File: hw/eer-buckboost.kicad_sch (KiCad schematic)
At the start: 58 parts, among them IC2001 LTC3779IFE#PBF, Q2001 BSC360N15NS3 G, Q2002 BSC360N15NS3 G, Q2003 BSC360N15NS3 G, Q2004 BSC360N15NS3 G, U2001 NVTFS6H888NLTAG, U2002 TLV9062xD

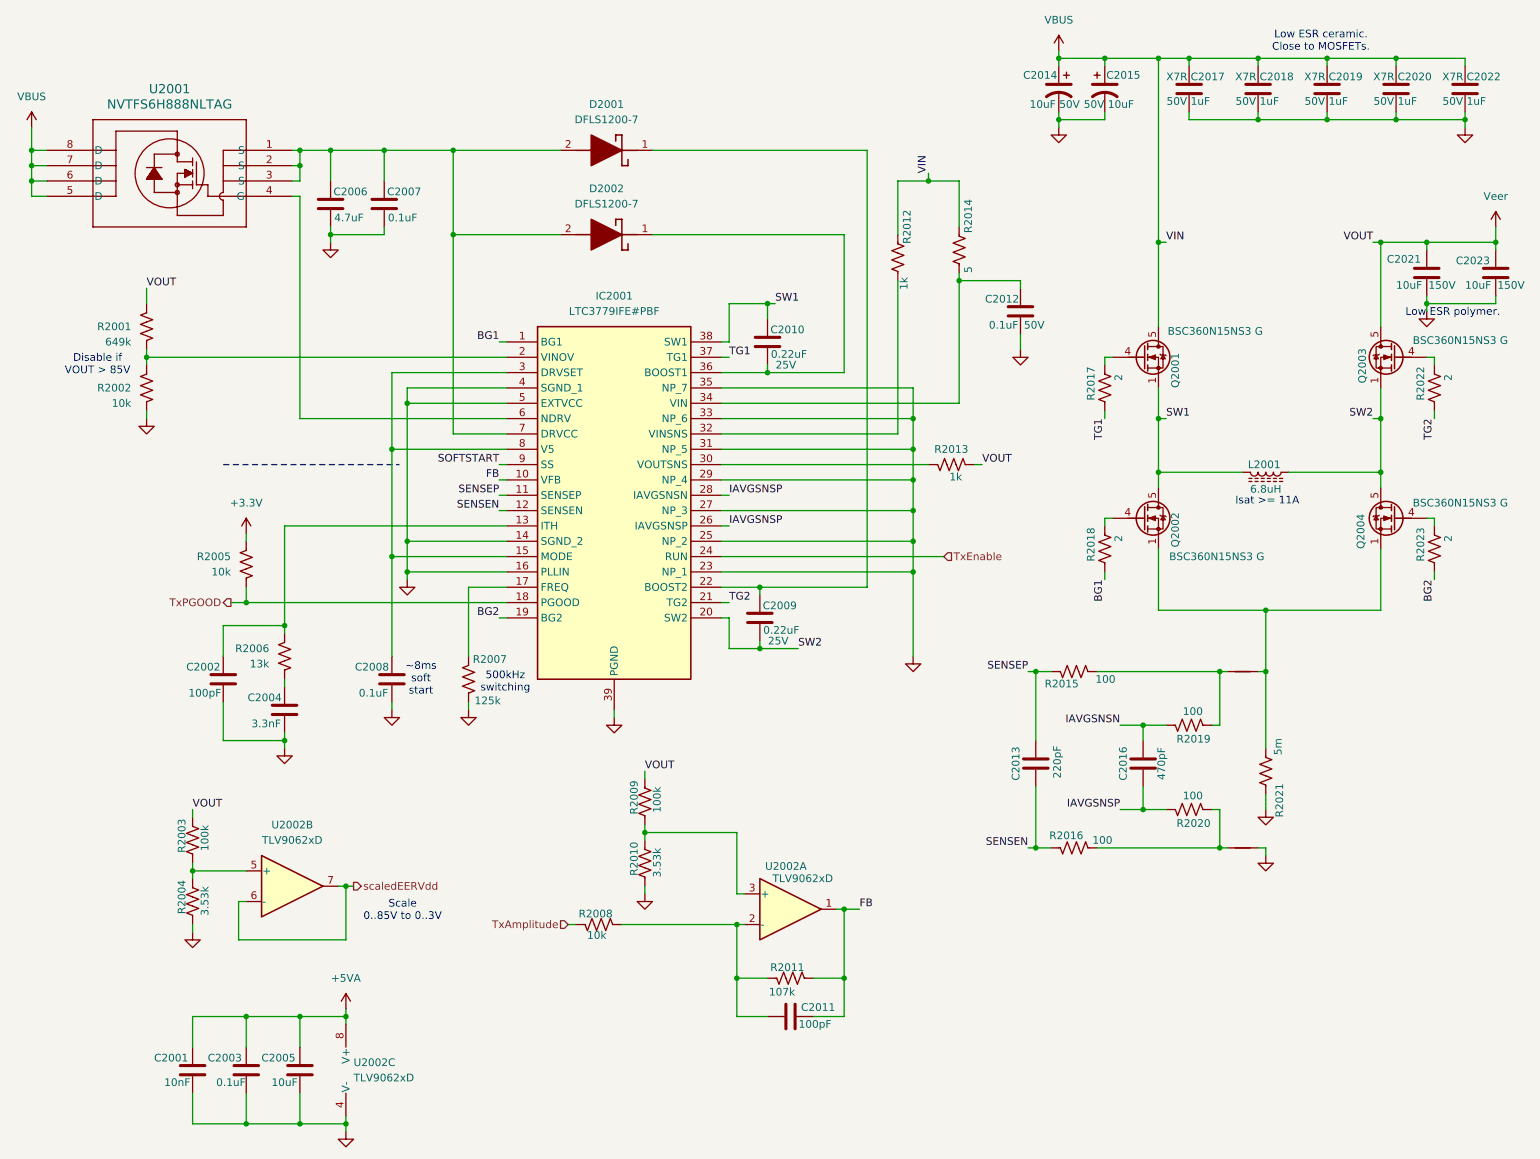
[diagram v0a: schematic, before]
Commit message: Schematic capture of the USBPD and +12V (+12V has priority) power scheme is "done". Have started working on RF deck mezzanine module but not yet divorced into another project
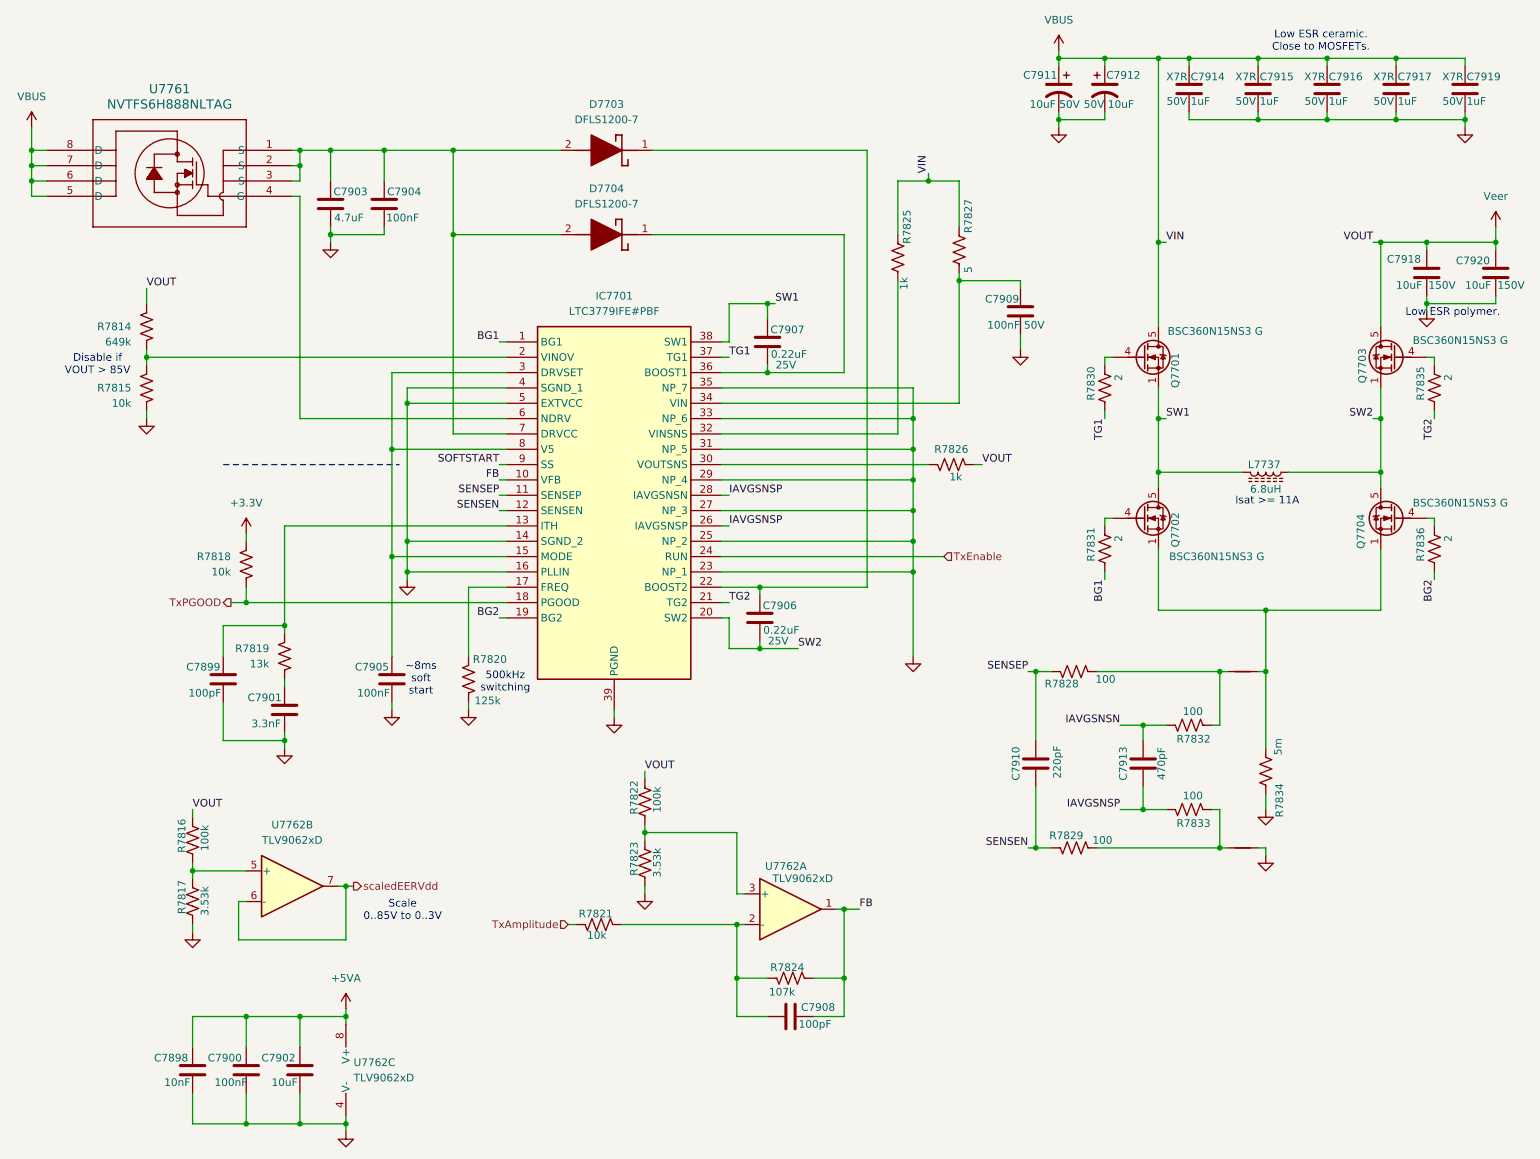
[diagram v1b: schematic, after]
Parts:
- C7900: renamed from C2003; value 0.1uF -> 100nF
- C7904: renamed from C2007; value 0.1uF -> 100nF
- C7905: renamed from C2008; value 0.1uF -> 100nF
- C7909: renamed from C2012; value 0.1uF -> 100nF
- renumbered C2001 to C7898, C2002 to C7899, C2004 to C7901, C2005 to C7902, C2006 to C7903, C2009 to C7906, C2010 to C7907, C2011 to C7908, C2013 to C7910, C2014 to C7911, C2015 to C7912, C2016 to C7913, C2017 to C7914, C2018 to C7915, C2019 to C7916, C2020 to C7917, C2021 to C7918, C2022 to C7919, C2023 to C7920, D2001 to D7703, D2002 to D7704, IC2001 to IC7701, L2001 to L7737, NT2001 to NT7701, NT2002 to NT7702, Q2001 to Q7701, Q2002 to Q7702, Q2003 to Q7703, Q2004 to Q7704, R2001 to R7814, R2002 to R7815, R2003 to R7816, R2004 to R7817, R2005 to R7818, R2006 to R7819, R2007 to R7820, R2008 to R7821, R2009 to R7822, R2010 to R7823, R2011 to R7824, R2012 to R7825, R2013 to R7826, R2014 to R7827, R2015 to R7828, R2016 to R7829, R2017 to R7830, R2018 to R7831, R2019 to R7832, R2020 to R7833, R2021 to R7834, R2022 to R7835, R2023 to R7836, U2001 to U7761, U2002 to U7762

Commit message: Last rites for 800 ohm rx preselector, and probably the RF deck which was stillborn
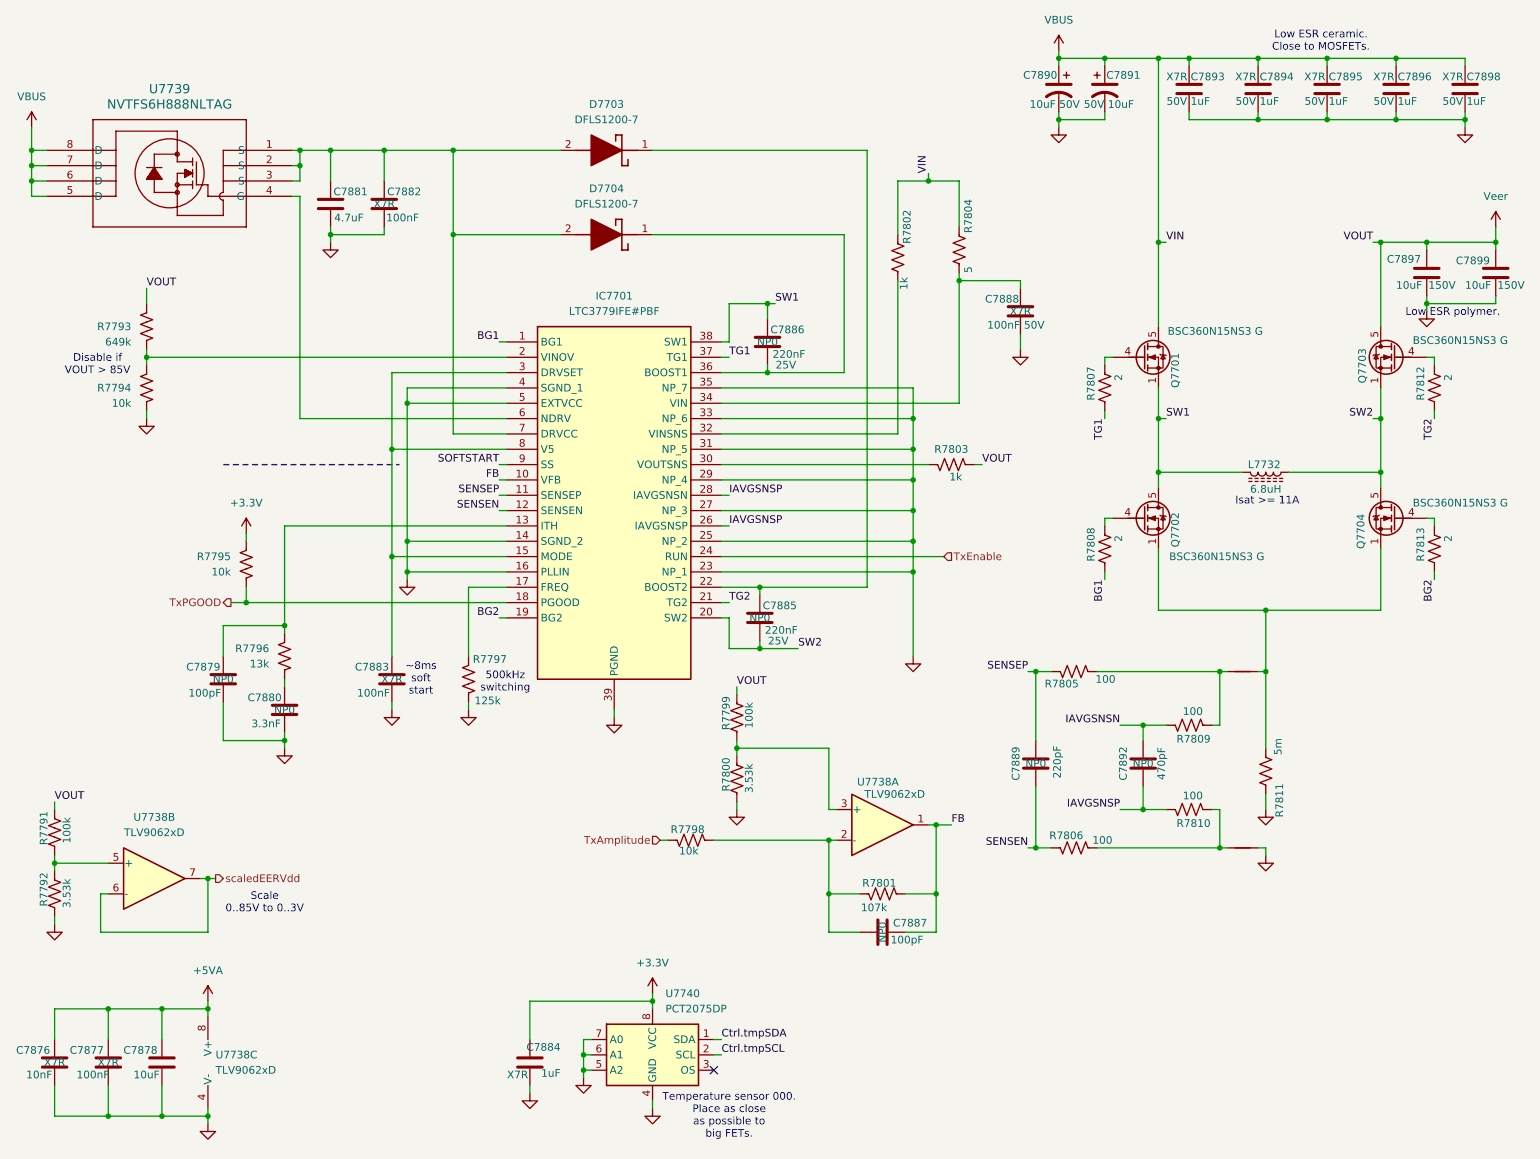
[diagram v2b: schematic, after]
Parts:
- added C7884: 1uF, Capacitor_SMD:C_0805_2012Metric, symbol Device:C
- added U7740: PCT2075DP, Package_SO:TSSOP-8_3x3mm_P0.65mm, symbol Sensor_Temperature:PCT2075DP
- C7876: renamed from C7898; cap-type (none) -> X7R
- C7877: renamed from C7900; cap-type (none) -> X7R
- C7879: renamed from C7899; footprint Capacitor_SMD:C_0603_1608Metric -> Capacitor_SMD:C_0201_0603Metric; cap-type (none) -> NP0
- C7880: renamed from C7901; footprint Capacitor_SMD:C_0805_2012Metric -> Capacitor_SMD:C_0201_0603Metric; cap-type (none) -> NP0
- C7882: renamed from C7904; cap-type (none) -> X7R
- C7883: renamed from C7905; cap-type (none) -> X7R
- C7885: renamed from C7906; value 0.22uF -> 220nF; cap-type (none) -> NP0
- C7886: renamed from C7907; value 0.22uF -> 220nF; cap-type (none) -> NP0
- C7887: renamed from C7908; footprint Capacitor_SMD:C_0603_1608Metric -> Capacitor_SMD:C_0201_0603Metric; cap-type (none) -> NP0
- C7888: renamed from C7909; cap-type (none) -> X7R
- C7889: renamed from C7910; footprint Capacitor_SMD:C_0805_2012Metric -> Capacitor_SMD:C_0201_0603Metric; cap-type (none) -> NP0
- C7892: renamed from C7913; footprint Capacitor_SMD:C_0805_2012Metric -> Capacitor_SMD:C_0201_0603Metric; cap-type (none) -> NP0
- renumbered C7902 to C7878, C7903 to C7881, C7911 to C7890, C7912 to C7891, C7914 to C7893, C7915 to C7894, C7916 to C7895, C7917 to C7896, C7918 to C7897, C7919 to C7898, C7920 to C7899, L7737 to L7732, R7816 to R7791, R7817 to R7792, R7814 to R7793, R7815 to R7794, R7818 to R7795, R7819 to R7796, R7820 to R7797, R7821 to R7798, R7822 to R7799, R7823 to R7800, R7824 to R7801, R7825 to R7802, R7826 to R7803, R7827 to R7804, R7828 to R7805, R7829 to R7806, R7830 to R7807, R7831 to R7808, R7832 to R7809, R7833 to R7810, R7834 to R7811, R7835 to R7812, R7836 to R7813, U7762 to U7738, U7761 to U7739
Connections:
- net +3.3V: now also C7884.1, U7740.8 (VCC)
- net GND: now also C7884.2, U7740.4 (GND), U7740.5 (A2), U7740.6 (A1), U7740.7 (A0)
- new net Ctrl.tmpSCL: U7740.2 (SCL)
- new net Ctrl.tmpSDA: U7740.1 (SDA)
- no-connect marks 0 -> 1
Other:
- note added: "Temperature sensor 000. Place as close as possible to big FETs."
- moved on the sheet: C7876, C7877, C7878, C7887, R7791, R7792, R7798, R7799, R7800, R7801, U7738A, U7738B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

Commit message: Fixed GPIO assignments. Fixed symbol for GRL2-2 relays.
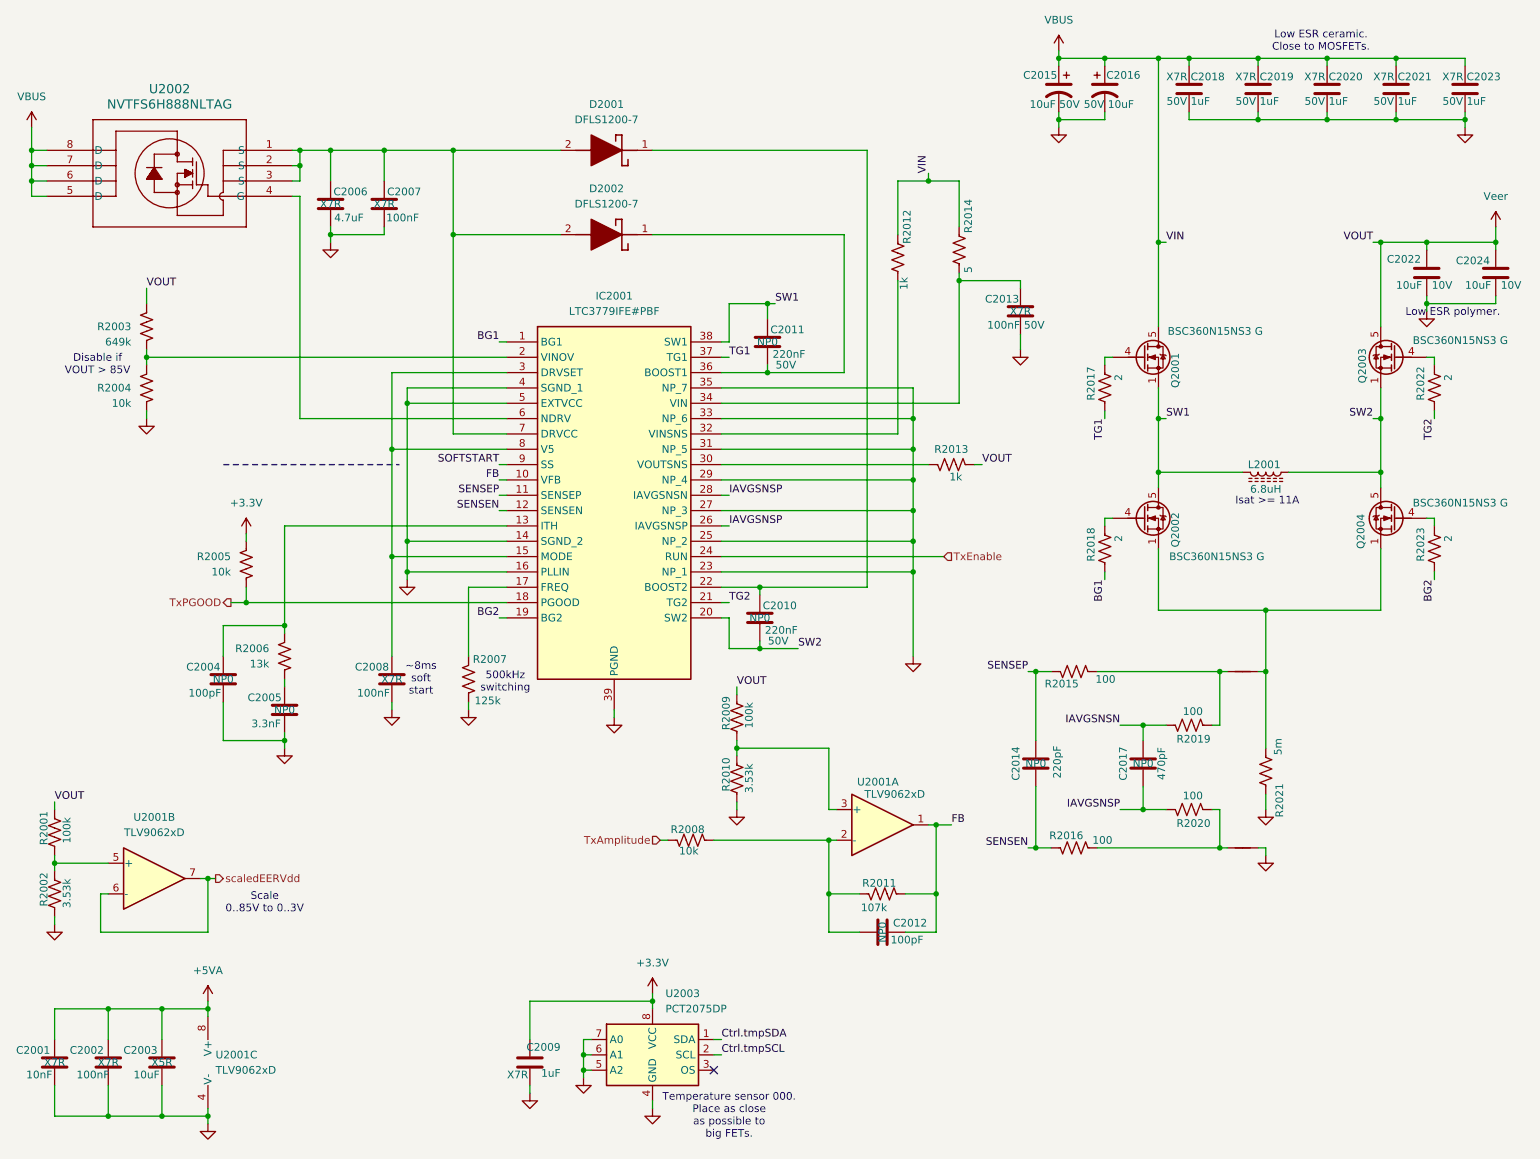
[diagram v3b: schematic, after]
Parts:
- C2001: renamed from C7876; working-voltage (none) -> 25V
- C2003: renamed from C7878; cap-type (none) -> X5R; working-voltage (none) -> 10V
- C2004: renamed from C7879; working-voltage (none) -> 50V
- C2005: renamed from C7880; working-voltage (none) -> 25V
- C2006: renamed from C7881; cap-type (none) -> X7R; working-voltage (none) -> 50V
- C2009: renamed from C7884; working-voltage (none) -> 50V
- C2010: renamed from C7885; working-voltage 25V -> 50V
- C2011: renamed from C7886; working-voltage 25V -> 50V
- C2012: renamed from C7887; working-voltage (none) -> 50V
- C2014: renamed from C7889; working-voltage (none) -> 25V
- C2017: renamed from C7892; working-voltage (none) -> 25V
- C2022: renamed from C7897; working-voltage 150V -> 10V
- C2024: renamed from C7899; working-voltage 150V -> 10V
- renumbered C7877 to C2002, C7882 to C2007, C7883 to C2008, C7888 to C2013, C7890 to C2015, C7891 to C2016, C7893 to C2018, C7894 to C2019, C7895 to C2020, C7896 to C2021, C7898 to C2023, D7703 to D2001, D7704 to D2002, IC7701 to IC2001, L7732 to L2001, NT7701 to NT2001, NT7702 to NT2002, Q7701 to Q2001, Q7702 to Q2002, Q7703 to Q2003, Q7704 to Q2004, R7791 to R2001, R7792 to R2002, R7793 to R2003, R7794 to R2004, R7795 to R2005, R7796 to R2006, R7797 to R2007, R7798 to R2008, R7799 to R2009, R7800 to R2010, R7801 to R2011, R7802 to R2012, R7803 to R2013, R7804 to R2014, R7805 to R2015, R7806 to R2016, R7807 to R2017, R7808 to R2018, R7809 to R2019, R7810 to R2020, R7811 to R2021, R7812 to R2022, R7813 to R2023, U7738 to U2001, U7739 to U2002, U7740 to U2003

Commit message: I think I have finished the relay conversion and 5V SPI I/O expander crap
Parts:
- renumbered C2001 to C7914, C2002 to C7915, C2003 to C7916, C2004 to C7917, C2005 to C7918, C2006 to C7919, C2007 to C7920, C2008 to C7921, C2009 to C7922, C2010 to C7923, C2011 to C7924, C2012 to C7925, C2013 to C7926, C2014 to C7927, C2015 to C7928, C2016 to C7929, C2017 to C7930, C2018 to C7931, C2019 to C7932, C2020 to C7933, C2021 to C7934, C2022 to C7935, C2023 to C7936, C2024 to C7937, D2001 to D7715, D2002 to D7716, IC2001 to IC7702, L2001 to L7735, NT2001 to NT7701, NT2002 to NT7702, Q2001 to Q7701, Q2002 to Q7702, Q2003 to Q7703, Q2004 to Q7704, R2001 to R7806, R2002 to R7807, R2003 to R7808, R2004 to R7809, R2005 to R7810, R2006 to R7811, R2007 to R7812, R2008 to R7813, R2009 to R7814, R2010 to R7815, R2011 to R7816, R2012 to R7817, R2013 to R7818, R2014 to R7819, R2015 to R7820, R2016 to R7821, R2017 to R7822, R2018 to R7823, R2019 to R7824, R2020 to R7825, R2021 to R7826, R2022 to R7827, R2023 to R7828, U2001 to U7751, U2002 to U7752, U2003 to U7753
